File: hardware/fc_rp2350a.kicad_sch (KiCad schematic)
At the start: 41 parts, among them Q5 AP1606, Q6 AP1606, U10 RP2354A, U11 TS2306A 240GF MSM 9_C2976675, X1 XTM25012000JT00351001

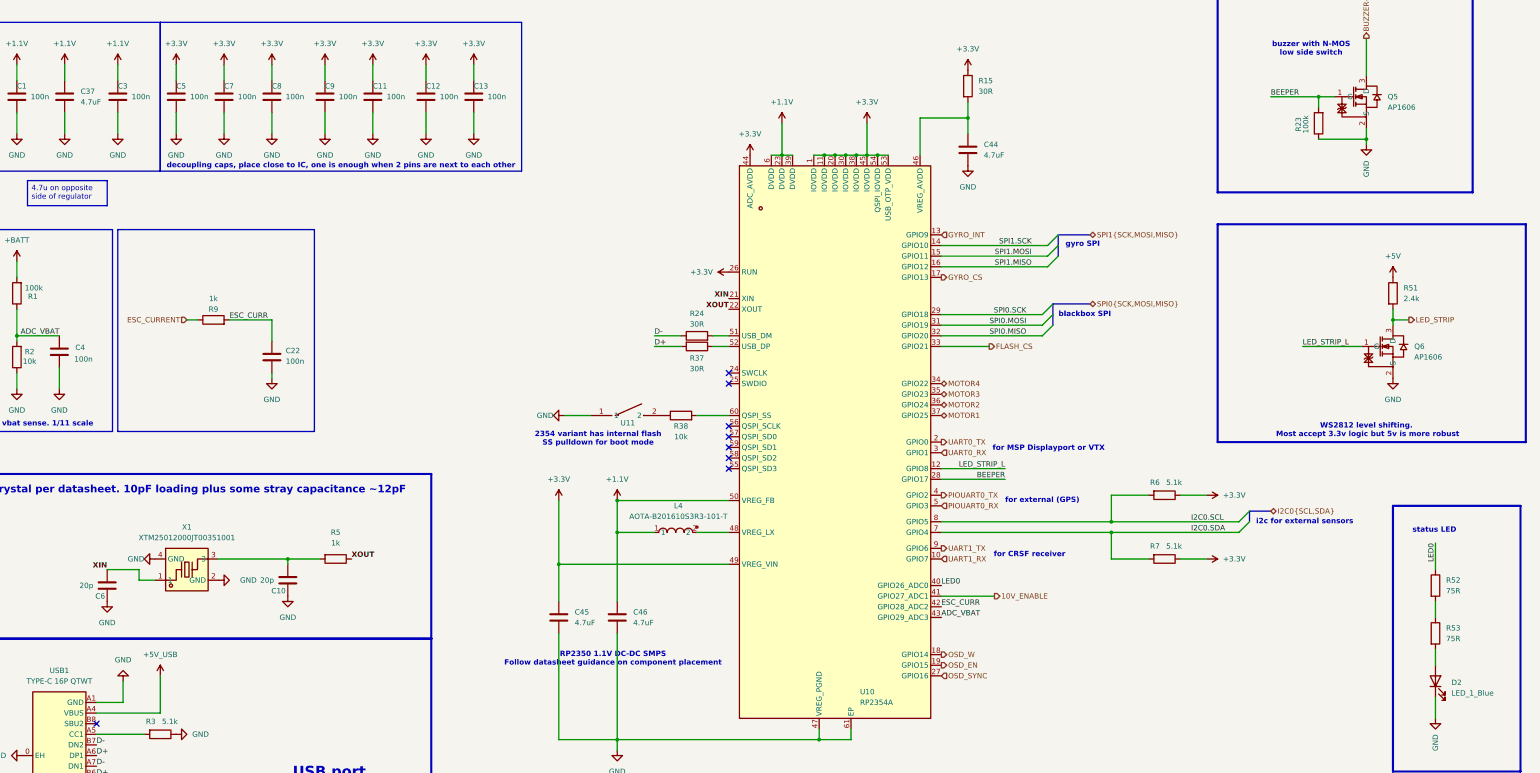
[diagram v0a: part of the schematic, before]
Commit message: Root sheet: place the sub-sheets; ESC as the 4in1 top sheet
esc_4in1.kicad_sch is OpenESC-20x20's 4in1-mini top sheet (battery input,
shunt and INA186 current sense, 12V/3V3 regulators, four ESC channel
instances). Its channel sub-sheet keeps its original file name ESC.kicad_sch
so the top sheet is untouched. Root sheet: Power, IMU, OSD, Blackbox, Pads,
RP2354A, ESC, RX placed, no wiring.
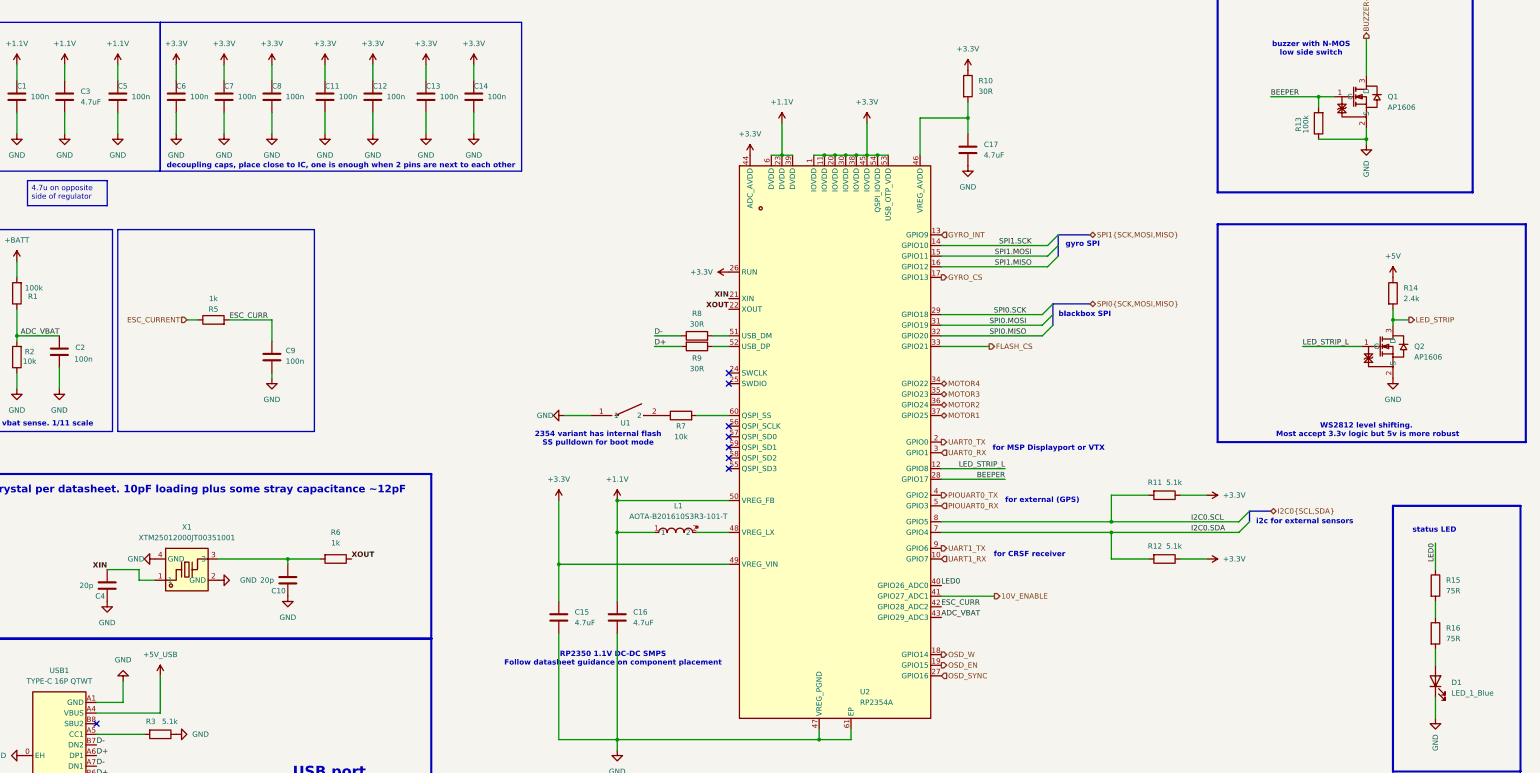
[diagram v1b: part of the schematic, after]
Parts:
- renumbered C9 to C11, C11 to C12, C12 to C13, C13 to C14, C45 to C15, C46 to C16, C44 to C17, C4 to C2, C37 to C3, C6 to C4, C3 to C5, C5 to C6, C22 to C9, D2 to D1, L4 to L1, Q5 to Q1, Q6 to Q2, R15 to R10, R6 to R11, R7 to R12, R23 to R13, R51 to R14, R52 to R15, R53 to R16, R9 to R5, R5 to R6, R38 to R7, R24 to R8, R37 to R9, U11 to U1, U10 to U2

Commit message: OpenAIO: master PCB with Base and Core islands routed, AIO_outline footprint+symbol in project lib
Save point before the two-board (LGA) split tooling.
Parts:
- C1, C10, C11, C12, C13, C14, C15, C16, C17, C2, C3, C4, C5, C6, C7, C8, C9, D1, R1, R10, R11, R12, R13, R14, R15, R16, R2, R3, R4, R5, R6, R7, R8, R9: KiLib_Generator (none) -> SMD_2terminal_chip_molded

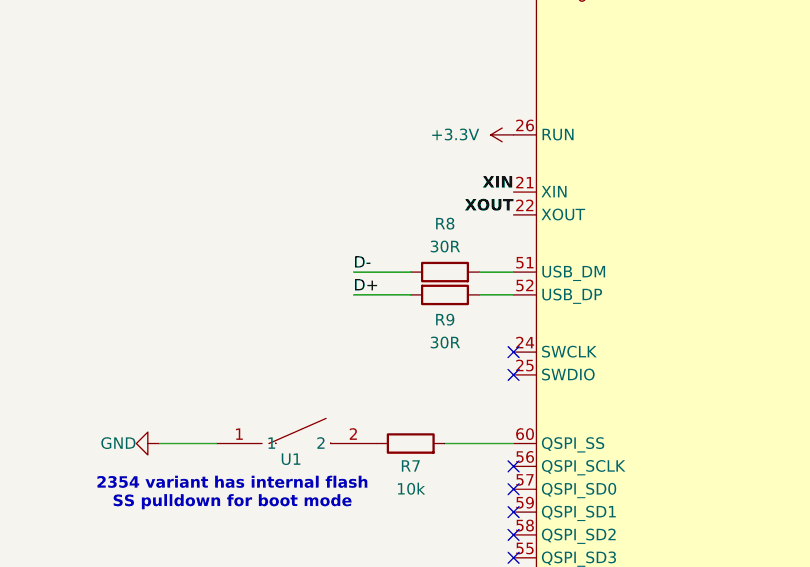
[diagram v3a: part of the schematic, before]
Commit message: OpenAIO: two-board stack tooling, Base + Core over an interior LGA
One project, one schematic, one master PCB; the shippable boards are derived.
tools/lga_gen.py: pin table -> Core_LGA_land, Core_LGA_pads (X pre-mirrored
for B.Cu), symbol Core_LGA, core_interface sheet with global labels.
tools/lga_wire_root.py: sheet on the root, global labels on the RP2354A wires,
USB_D+/- in fc_rp2350a, root CURR hier label made global (closes the CSA link).
tools/lga_place.py: J90 on the Base, J91 flipped on the Core, paths set.
tools/split_boards.py: export/OpenAIO-Base and -Core, DRC, Core STEP as J90
3D model plus outline shadow in the master. USB netclass patterns *D+/*D-.
AGENTS.md: architecture, derived boards, layout rules.
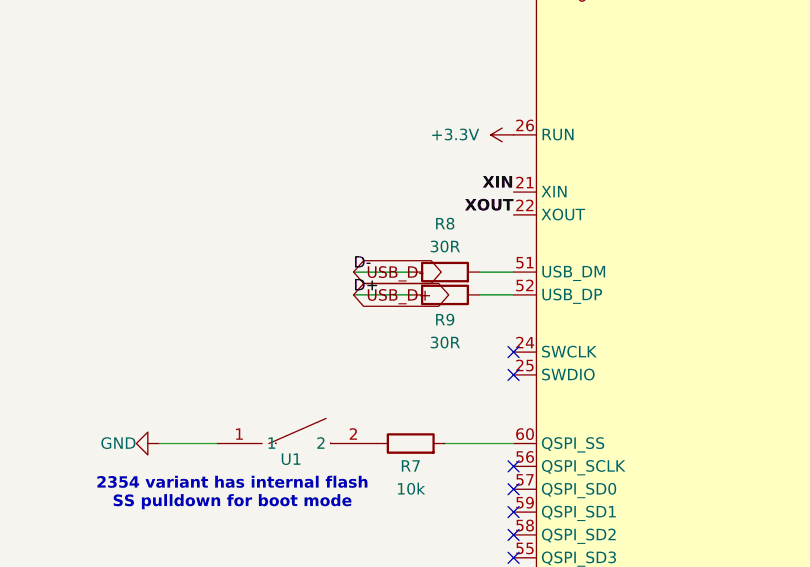
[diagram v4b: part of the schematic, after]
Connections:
- net D+ renamed USB_D+
- net D- renamed USB_D-
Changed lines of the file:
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@@
+		)
+	)
+	(global_label "USB_D+"
+		(shape bidirectional)
+		(at 252.73 190.5 0)
+		(effects
+			(font
+				(size 1.27 1.27)
+			)
+			(justify left)
+		)
+	)
+	(global_label "USB_D-"
+		(shape bidirectional)
+		(at 252.73 187.96 0)
+		(effects
+			(font
+				(size 1.27 1.27)
+			)
+			(justify left)
 		)
 	)
